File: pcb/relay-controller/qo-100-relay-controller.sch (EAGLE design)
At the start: 125 parts, among them CON1 4P-SH-SIDE, CON10 2EDG-2P-5MM, CON11 2EDG-2P-5MM, CON12 2EDG-2P-5MM, CON13 2EDG-2P-5MM, CON14 2EDG-2P-5MM, CON2 2EDG-2P-5MM, CON3 2EDG-2P-5MM, CON4 2EDG-2P-5MM, CON5 2EDG-2P-5MM, CON6 2EDG-2P-5MM, CON7 2EDG-2P-5MM, CON8 2EDG-2P-5MM, CON9 2EDG-2P-5MM, Q1 AO3400, Q10 AO3400, Q11 AO3400, Q12 AO3400, Q2 AO3400, Q3 AO3400, Q4 AO3400, Q5 AO3400, Q6 AO3400, Q7 AO3400, Q8 AO3400, Q9 AO3400, U1 MCP1792-3.3, U2 MCP23017

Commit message: Change IO expander to MCU in relay controller to allow later flexibility
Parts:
- removed SJ1, SJ2, SJ3: (no value), Solder Jumper:SJ2S
- added C24: 470pF, Capacitor:CAPACITOR-0603
- added C7: 1uF, Capacitor:CAPACITOR-0603
- added C8, C9: 100nF, Capacitor:CAPACITOR-0603
- added D26: LED0603, LED:LED0603
- added R13, R53: 10K Ohms, Resistor:RESISTOR-0603
- added R14: 330 Ohms, Resistor:RESISTOR-0603
- added R15, R16: 1K Ohms, Resistor:RESISTOR-0603
- added R54: 100K Ohms, Resistor:RESISTOR-0603
- added TC1: TC2050-IDC, TagConnect:TC2050-IDC
- U2: value MCP23017 -> EFM32TG11B120F128GM32; device Microchip:MCP23017 -> EFM32:EFM32TG11B120F128GM32
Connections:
- removed net IO_A0: SJ1.2, U2.A0
- removed net IO_A1: SJ2.2, U2.A1
- removed net IO_A2: SJ3.2, U2.A2
- new net !RESET: R13.1, TC1-10(!RESET!).S, U2.!RESET
- new net LED: R14.2, U2.PE11
- new net N$14: C7.C1, U2.DECOUPLE
- new net N$15: D26.A, R14.1
- new net SWCLK: TC1-4(TCK/SWCLK).S, U2.PF0
- new net SWDIO: TC1-2(TMS/SWDIO).S, U2.PF1
- new net SWO: TC1-6(TDO/SWO).S, U2.PF2
- new net VIN_VSENSE: C24.C1, R53.2, R54.1, U2.PB11
- net 3V3: now also C8.C1, C9.C1, R13.2, R15.2, R16.2, TC1-1(VTARGET).S, U2.AVDD@0, U2.AVDD@1, U2.DVDD, U2.IOVDD0@0, U2.IOVDD0@1, U2.IOVDD0@2; no longer SJ1.3, SJ2.3, SJ3.3, U2.!RESET, U2.VDD
- net GND: now also C24.C2, C7.C2, C8.C2, C9.C2, D26.C, R53.1, TC1-3(GND).S, U2.VSS@0; no longer SJ1.1, SJ2.1, SJ3.1, U2.VSS
- net I2C_SCL: now also R15.1, U2.PE13; no longer U2.SCL
- net I2C_SDA: now also R16.1, U2.PE12; no longer U2.SDA
- net R0: now also U2.PB8; no longer U2.GPA0
- net R1: now also U2.PB7; no longer U2.GPA1
- net R10: now also U2.PD5; no longer U2.GPB4
- net R11: now also U2.PD4; no longer U2.GPB5
- net R2: now also U2.PC1; no longer U2.GPA2
- net R3: now also U2.PA2; no longer U2.GPA3
- net R4: now also U2.PA1; no longer U2.GPA4
- net R5: now also U2.PA0; no longer U2.GPA5
- net R6: now also U2.PC14; no longer U2.GPB0
- net R7: now also U2.PC13; no longer U2.GPB1
- net R8: now also U2.PD7; no longer U2.GPB2
- net R9: now also U2.PD6; no longer U2.GPB3
- net VIN: now also R54.2
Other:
- moved on the sheet: C3, C6, CON10-1, CON10-2, CON11-1, CON11-2, CON12-1, CON12-2, CON13-1, CON13-2, CON14-1, CON14-2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

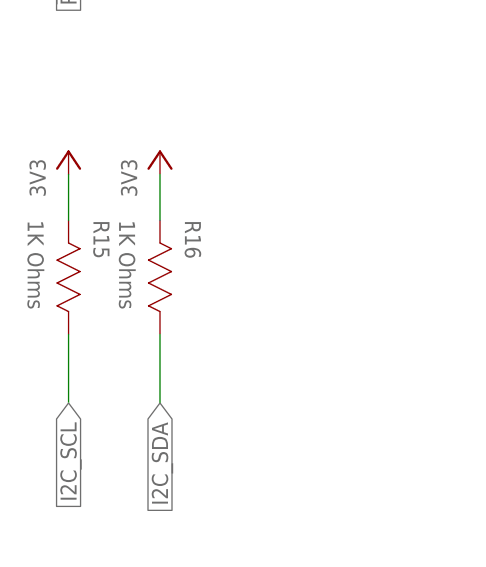
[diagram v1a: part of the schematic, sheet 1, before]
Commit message: Update I2C slave resistors to minimize load effect when powered down
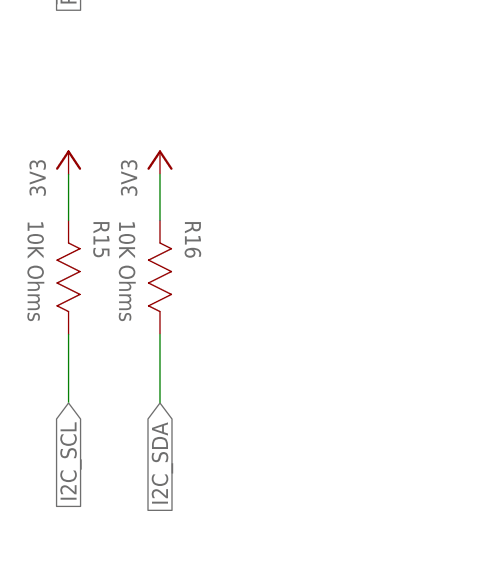
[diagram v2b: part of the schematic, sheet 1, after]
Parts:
- R15, R16: value 1K Ohms -> 10K Ohms
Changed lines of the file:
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@@
 <part name="3V8" library="Supply Symbol" deviceset="3V3" device=""/>
 <part name="U2" library="EFM32" deviceset="EFM32TG11B1*M32" device="" technology="20F128G"/>
-<part name="R15" library="Resistor" deviceset="RESISTOR" device="-0603" value="1K Ohms"/>
+<part name="R15" library="Resistor" deviceset="RESISTOR" device="-0603" value="10K Ohms"/>
 <part name="3V21" library="Supply Symbol" deviceset="3V3" device=""/>
-<part name="R16" library="Resistor" deviceset="RESISTOR" device="-0603" value="1K Ohms"/>
+<part name="R16" library="Resistor" deviceset="RESISTOR" device="-0603" value="10K Ohms"/>
 <part name="3V22" library="Supply Symbol" deviceset="3V3" device=""/>
 <part name="R53" library="Resistor" deviceset="RESISTOR" device="-0603" value="10K Ohms"/>
